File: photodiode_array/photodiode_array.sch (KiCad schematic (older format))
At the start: 31 parts, among them U1 LM741, U2 LM324, U3 LM324

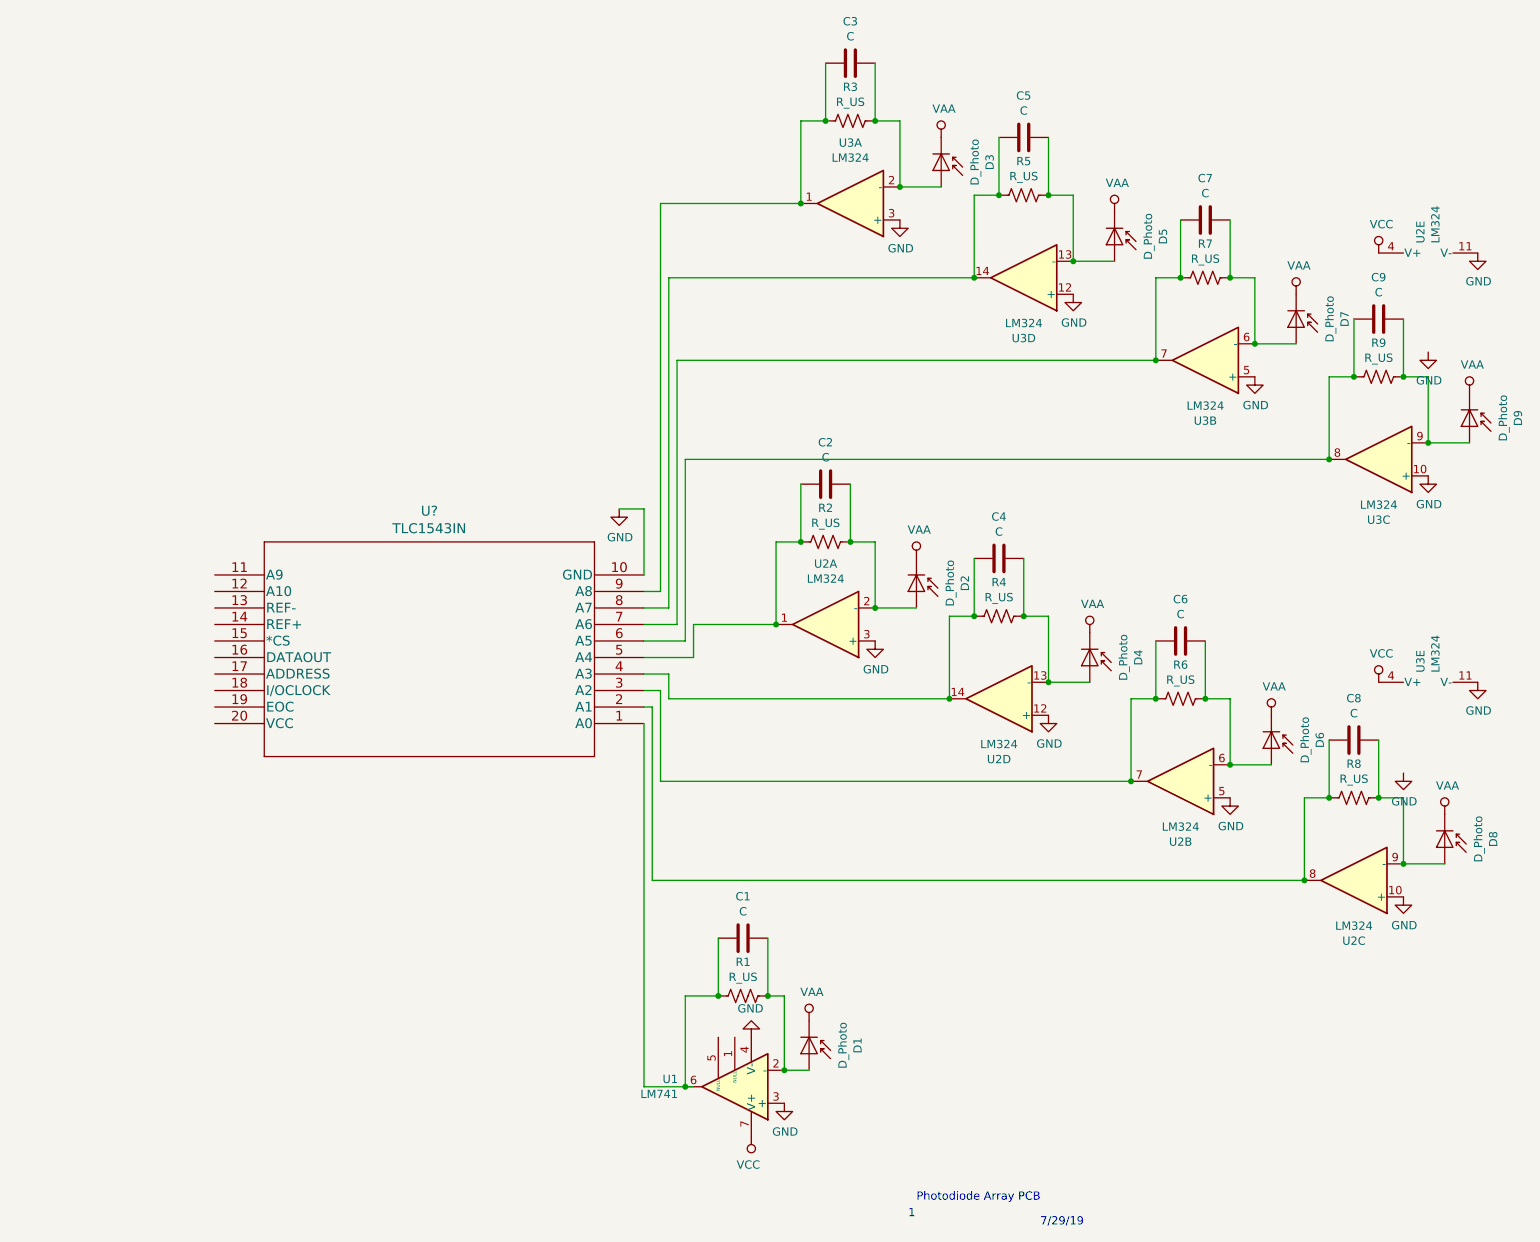
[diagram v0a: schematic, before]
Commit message: adding footprints
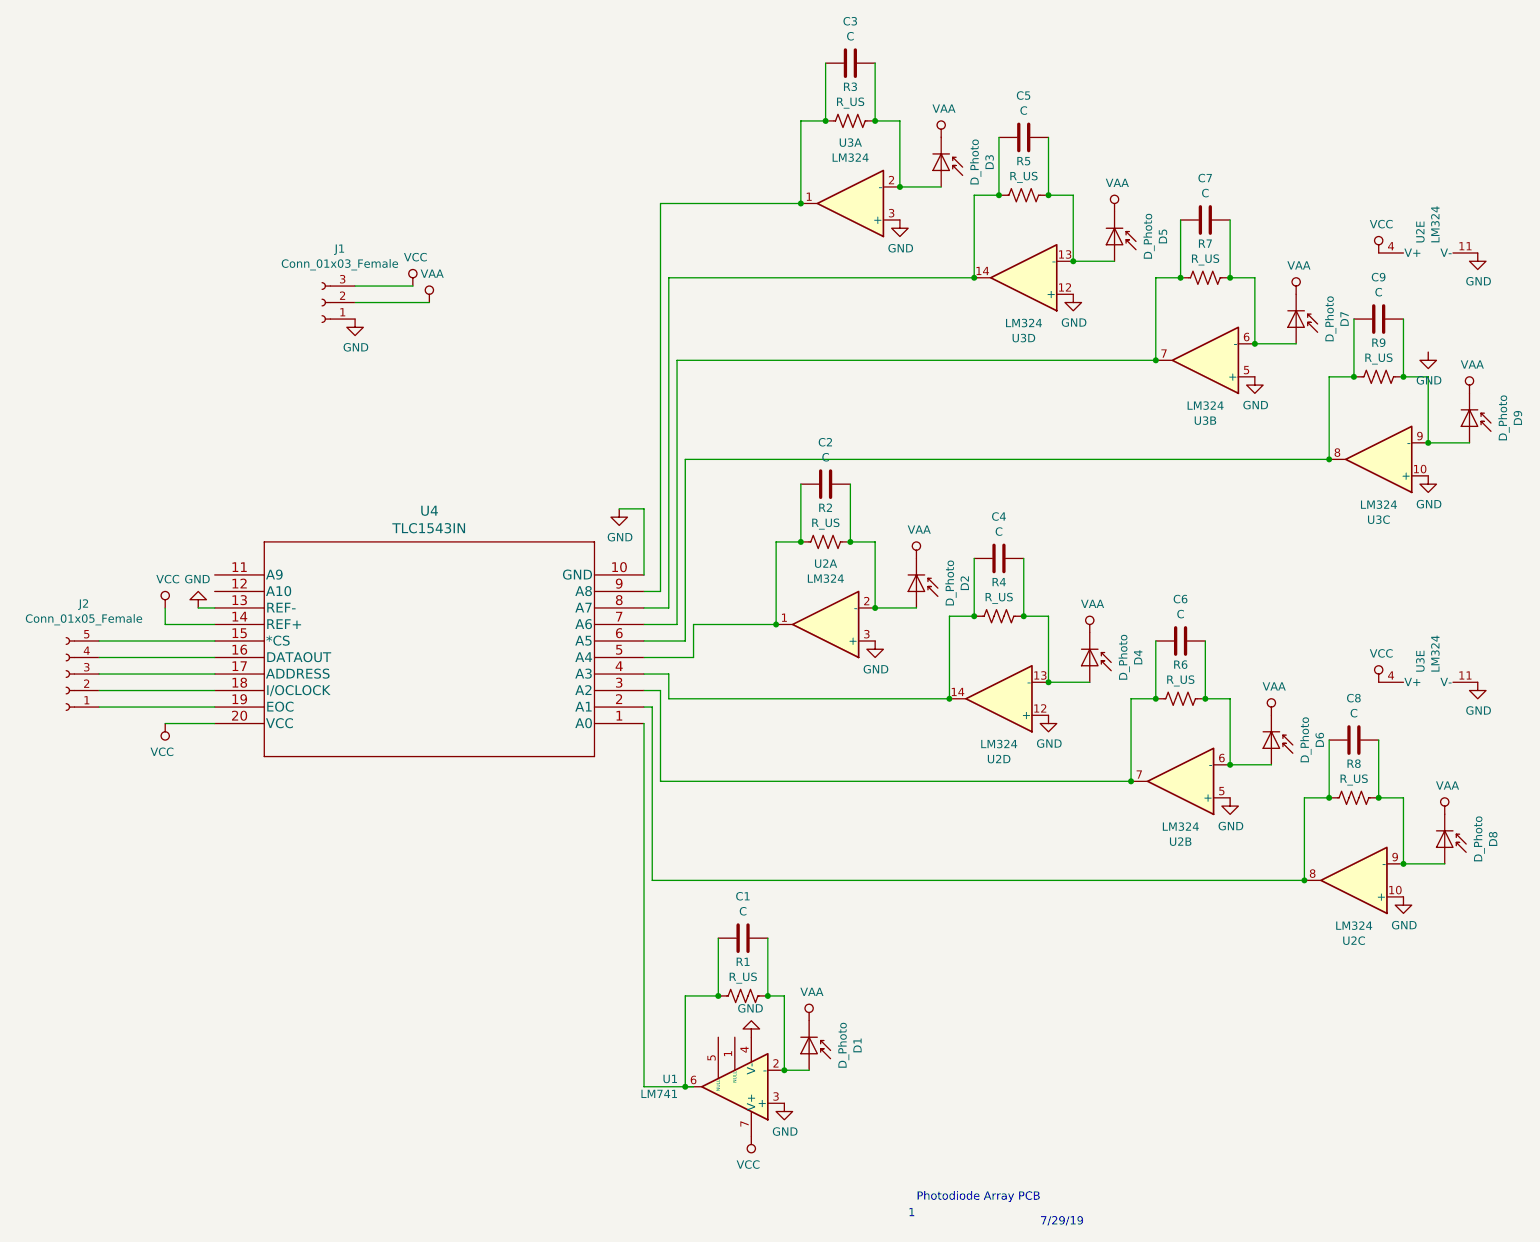
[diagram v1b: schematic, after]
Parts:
- added J1: Conn_01x03_Female, Connector_PinSocket_1.00mm:PinSocket_1x03_P1.00mm_Vertical, symbol Connector:Conn_01x03_Female
- added J2: Conn_01x05_Female, Connector_PinSocket_1.00mm:PinSocket_1x05_P1.00mm_Vertical, symbol Connector:Conn_01x05_Female
- D1, D2, D3, D4, D5, D6, D7, D8, D9: footprint (none) -> Diode_THT:D_DO-201AD_P3.81mm_Vertical_AnodeUp
- gave numbers to parts that had none: 1
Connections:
- net GND: now also U4.13 (REF-), J1.1 (Pin_1)
- net VAA: now also J1.2 (Pin_2)
- net VCC: now also U4.14 (REF+), U4.20 (VCC), J1.3 (Pin_3)
- net at U4.15 (*CS): now also J2.5 (Pin_5)
- net at U4.16 (DATAOUT): now also J2.4 (Pin_4)
- net at U4.17 (ADDRESS): now also J2.3 (Pin_3)
- net at U4.18 (I/OCLOCK): now also J2.2 (Pin_2)
- net at U4.19 (EOC): now also J2.1 (Pin_1)
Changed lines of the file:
@@
 F 0 "D7" H 9600 2495 50  0000 C CNN
 F 1 "D_Photo" H 9600 2404 50  0000 C CNN
-F 2 "" H 9600 2200 50  0001 C CNN
+F 2 "Diode_THT:D_DO-201AD_P3.81mm_Vertical_AnodeUp" H 9600 2200 50  0001 C CNN
 F 3 "~" H 9600 2200 50  0001 C CNN
 	1    9650 2200
@@
 F 0 "D9" H 10650 3095 50  0000 C CNN
 F 1 "D_Photo" H 10650 3004 50  0000 C CNN
-F 2 "" H 10650 2800 50  0001 C CNN
+F 2 "Diode_THT:D_DO-201AD_P3.81mm_Vertical_AnodeUp" H 10650 2800 50  0001 C CNN
 F 3 "~" H 10650 2800 50  0001 C CNN
 	1    10700 2800
@@
 F 0 "D3" H 7450 1545 50  0000 C CNN
 F 1 "D_Photo" H 7450 1454 50  0000 C CNN
-F 2 "" H 7450 1250 50  0001 C CNN
+F 2 "Diode_THT:D_DO-201AD_P3.81mm_Vertical_AnodeUp" H 7450 1250 50  0001 C CNN
 F 3 "~" H 7450 1250 50  0001 C CNN
 	1    7500 1250
@@
 F 0 "D1" H 6650 6895 50  0000 C CNN
 F 1 "D_Photo" H 6650 6804 50  0000 C CNN
-F 2 "" H 6650 6600 50  0001 C CNN
+F 2 "Diode_THT:D_DO-201AD_P3.81mm_Vertical_AnodeUp" H 6650 6600 50  0001 C CNN
 F 3 "~" H 6650 6600 50  0001 C CNN
 	1    6700 6600
@@
 F 0 "D5" H 8500 1995 50  0000 C CNN
 F 1 "D_Photo" H 8500 1904 50  0000 C CNN
-F 2 "" H 8500 1700 50  0001 C CNN
+F 2 "Diode_THT:D_DO-201AD_P3.81mm_Vertical_AnodeUp" H 8500 1700 50  0001 C CNN
 F 3 "~" H 8500 1700 50  0001 C CNN
 	1    8550 1700
@@
 F 0 "D6" H 9450 5045 50  0000 C CNN
 F 1 "D_Photo" H 9450 4954 50  0000 C CNN
-F 2 "" H 9450 4750 50  0001 C CNN
+F 2 "Diode_THT:D_DO-201AD_P3.81mm_Vertical_AnodeUp" H 9450 4750 50  0001 C CNN
 F 3 "~" H 9450 4750 50  0001 C CNN
 	1    9500 4750
@@
 F 0 "D2" H 7300 4095 50  0000 C CNN
 F 1 "D_Photo" H 7300 4004 50  0000 C CNN
-F 2 "" H 7300 3800 50  0001 C CNN
+F 2 "Diode_THT:D_DO-201AD_P3.81mm_Vertical_AnodeUp" H 7300 3800 50  0001 C CNN
 F 3 "~" H 7300 3800 50  0001 C CNN
 	1    7350 3800
@@
 F 0 "D4" H 8350 4545 50  0000 C CNN
 F 1 "D_Photo" H 8350 4454 50  0000 C CNN
-F 2 "" H 8350 4250 50  0001 C CNN
+F 2 "Diode_THT:D_DO-201AD_P3.81mm_Vertical_AnodeUp" H 8350 4250 50  0001 C CNN
 F 3 "~" H 8350 4250 50  0001 C CNN
 	1    8400 4250
@@
 $EndComp
 $Comp
-L power:GND #PWR0122
-U 1 1 5D594F28
-P 10300 4900
-F 0 "#PWR0122" H 10300 4650 50  0001 C CNN
-F 1 "GND" H 10305 4727 50  0000 C CNN
-F 2 "" H 10300 4900 50  0001 C CNN
-F 3 "" H 10300 4900 50  0001 C CNN
-	1    10300 4900
-	1    0    0    -1
-$EndComp
-$Comp
 L power:VAA #PWR0123
 U 1 1 5D594F0F
@@
 F 0 "D8" H 10500 5645 50  0000 C CNN
 F 1 "D_Photo" H 10500 5554 50  0000 C CNN
-F 2 "" H 10500 5350 50  0001 C CNN
+F 2 "Diode_THT:D_DO-201AD_P3.81mm_Vertical_AnodeUp" H 10500 5350 50  0001 C CNN
 F 3 "~" H 10500 5350 50  0001 C CNN
 	1    10550 5350
@@
 Wire Wire Line
 	5700 6800 5700 4600
-$Comp
-L TLC1543IN:TLC1543IN U?
-U 1 1 5D4128DE
-P 5700 4600
-F 0 "U?" H 7000 3313 60  0000 C CNN
-F 1 "TLC1543IN" H 7000 3419 60  0000 C CNN
-F 2 "N20" H 7000 4840 60  0001 C CNN
-F 3 "" H 5700 4600 60  0000 C CNN
-	1    5700 4600
-	-1   0    0    1
-$EndComp
 Wire Wire Line
 	5800 4400 5700 4400
@@
 	5700 3300 5550 3300
 $Comp
-L power:GND #PWR?
+L power:GND #PWR0122
 U 1 1 5D4692B1
 P 5550 3300
-F 0 "#PWR?" H 5550 3050 50  0001 C CNN
+F 0 "#PWR0122" H 5550 3050 50  0001 C CNN
 F 1 "GND" H 5555 3127 50  0000 C CNN
 F 2 "" H 5550 3300 50  0001 C CNN
@@
 	1    0    0    -1
 $EndComp
+$Comp
+L power:GND #PWR0127
+U 1 1 5D42D101
+P 3000 3900
+F 0 "#PWR0127" H 3000 3650 50  0001 C CNN
+F 1 "GND" H 3005 3727 50  0000 C CNN
+F 2 "" H 3000 3900 50  0001 C CNN
+F 3 "" H 3000 3900 50  0001 C CNN
+	1    3000 3900
+	-1   0    0    1
+$EndComp
+Wire Wire Line
+	3000 3900 3100 3900
+$Comp
+L power:VCC #PWR0128
+U 1 1 5D432843
+P 2800 3900
+F 0 "#PWR0128" H 2800 3750 50  0001 C CNN
+F 1 "VCC" H 2817 4073 50  0000 C CNN
+F 2 "" H 2800 3900 50  0001 C CNN
+F 3 "" H 2800 3900 50  0001 C CNN
+	1    2800 3900
+	1    0    0    -1
+$EndComp
+Wire Wire Line
+	3100 4000 2800 4000
+Wire Wire Line
+	2800 4000 2800 3900
+$Comp
+L power:VCC #PWR0129
+U 1 1 5D43C801
+P 2800 4600
+F 0 "#PWR0129" H 2800 4450 50  0001 C CNN
+F 1 "VCC" H 2818 4773 50  0000 C CNN
+F 2 "" H 2800 4600 50  0001 C CNN
+F 3 "" H 2800 4600 50  0001 C CNN
+	1    2800 4600
+	-1   0    0    1
+$EndComp
+Wire Wire Line
+	2800 4600 3100 4600
+$Comp
+L Connector:Conn_01x05_Female J2
+U 1 1 5D49638C
+P 2200 4300
+F 0 "J2" H 2092 3875 50  0000 C CNN
+F 1 "Conn_01x05_Female" H 2092 3966 50  0000 C CNN
+F 2 "Connector_PinSocket_1.00mm:PinSocket_1x05_P1.00mm_Vertical" H 2200 4300 50  0001 C CNN
+F 3 "~" H 2200 4300 50  0001 C CNN
+	1    2200 4300
+	-1   0    0    1
+$EndComp
+$Comp
+L Connector:Conn_01x03_Female J1
+U 1 1 5D49ADD4
+P 3750 2050
+F 0 "J1" H 3642 1725 50  0000 C CNN
+F 1 "Conn_01x03_Female" H 3642 1816 50  0000 C CNN
+F 2 "Connector_PinSocket_1.00mm:PinSocket_1x03_P1.00mm_Vertical" H 3750 2050 50  0001 C CNN
+F 3 "~" H 3750 2050 50  0001 C CNN
+	1    3750 2050
+	-1   0    0    1
+$EndComp
+$Comp
+L power:GND #PWR0130
+U 1 1 5D49D81A
+P 3950 2150
+F 0 "#PWR0130" H 3950 1900 50  0001 C CNN
+F 1 "GND" H 3955 1977 50  0000 C CNN
+F 2 "" H 3950 2150 50  0001 C CNN
+F 3 "" H 3950 2150 50  0001 C CNN
+	1    3950 2150
+	1    0    0    -1
+$EndComp
+$Comp
+L power:VCC #PWR0131
+U 1 1 5D49FEE9
+P 4300 1950
+F 0 "#PWR0131" H 4300 1800 50  0001 C CNN
+F 1 "VCC" H 4317 2123 50  0000 C CNN
+F 2 "" H 4300 1950 50  0001 C CNN
+F 3 "" H 4300 1950 50  0001 C CNN
+	1    4300 1950
+	1    0    0    -1
+$EndComp
+$Comp
+L power:VAA #PWR0132
+U 1 1 5D4A16BA
+P 4400 2050
+F 0 "#PWR0132" H 4400 1900 50  0001 C CNN
+F 1 "VAA" H 4417 2223 50  0000 C CNN
+F 2 "" H 4400 2050 50  0001 C CNN
+F 3 "" H 4400 2050 50  0001 C CNN
+	1    4400 2050
+	1    0    0    -1
+$EndComp
+Wire Wire Line
+	3950 1950 4300 1950
+Wire Wire Line
+	4400 2050 3950 2050
+Wire Wire Line
+	2400 4100 3100 4100
+Wire Wire Line
+	2400 4200 3100 4200
+Wire Wire Line
+	3100 4300 2400 4300
+Wire Wire Line
+	2400 4400 3100 4400
+Wire Wire Line
+	3100 4500 2400 4500
+$Comp
+L TLC1543IN:TLC1543IN U4
+U 1 1 5D4128DE
+P 5700 4600
+F 0 "U4" H 7000 3313 60  0000 C CNN
+F 1 "TLC1543IN" H 7000 3419 60  0000 C CNN
+F 2 "N20" H 7000 4840 60  0001 C CNN
+F 3 "http://www.ti.com/lit/ds/symlink/tlc1543.pdf" H 5700 4600 60  0001 C CNN
+	1    5700 4600
+	-1   0    0    1
+$EndComp
 $EndSCHEMATC
